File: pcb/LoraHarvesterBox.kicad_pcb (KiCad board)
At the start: 4 copper layers, 48 x 45.5 mm, 44 parts, among them J1 Conn_01x02_Pin, J2 Conn_01x02_Pin, J3 Conn_01x02_Pin, J4 Conn_01x04_Socket, J5 Conn_01x04_Socket, J6 Conn_01x04_Socket, J7 Conn_01x04_Socket, J8 Conn_01x06_Socket, J9 Conn_01x08_Socket, SW1 SSSS811101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

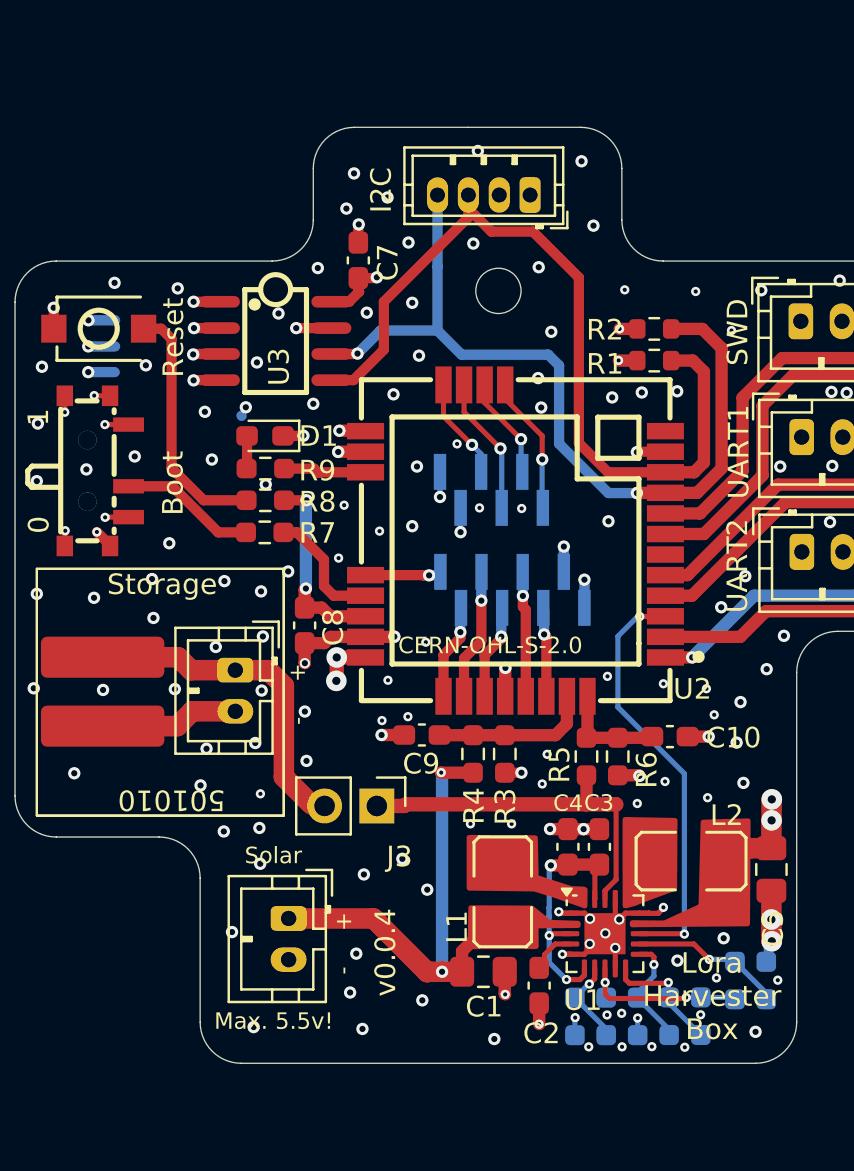
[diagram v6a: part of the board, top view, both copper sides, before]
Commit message: sch, doc: make I2C connector JST-ZH, move mounting hole
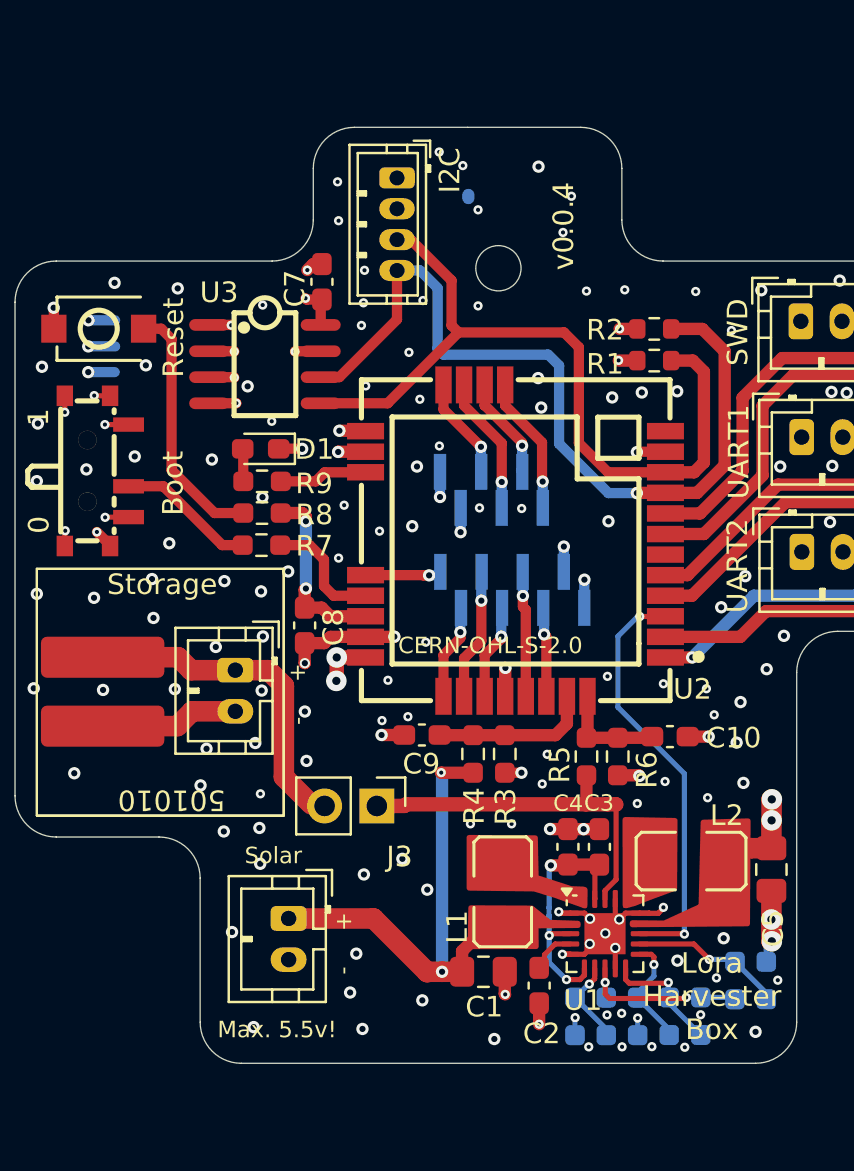
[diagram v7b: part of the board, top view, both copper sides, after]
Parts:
- moved J7 6.52 mm to (119.6, 57.0), turned to -90 degrees
- moved C7 2.05 mm to (115.9, 62.0)
- moved U3 1.24 mm to (113.2, 66.0)
- moved H1 1.10 mm to (124.5, 61.4)
- moved D1 0.66 mm to (112.9, 70.1)
- moved R8 0.64 mm to (113.0, 73.2)
- moved R7 0.64 mm to (113.0, 74.8)
- moved R9 0.64 mm to (113.0, 71.7)
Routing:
- net /SDA: track 41.5 -> 38.2 mm
- net +3V0: track 14.8 -> 13.3 mm
- net Net-(J8-Pin_6): track 6.01 -> 6.74 mm
- net /RST: track 9.48 -> 8.87 mm
- net /SCL: track 41.4 -> 40.8 mm, vias 2 -> 1
